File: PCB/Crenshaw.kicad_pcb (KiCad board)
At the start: 2 copper layers, 44.5 x 37 mm, 7 parts, among them J1 In, J2 Out

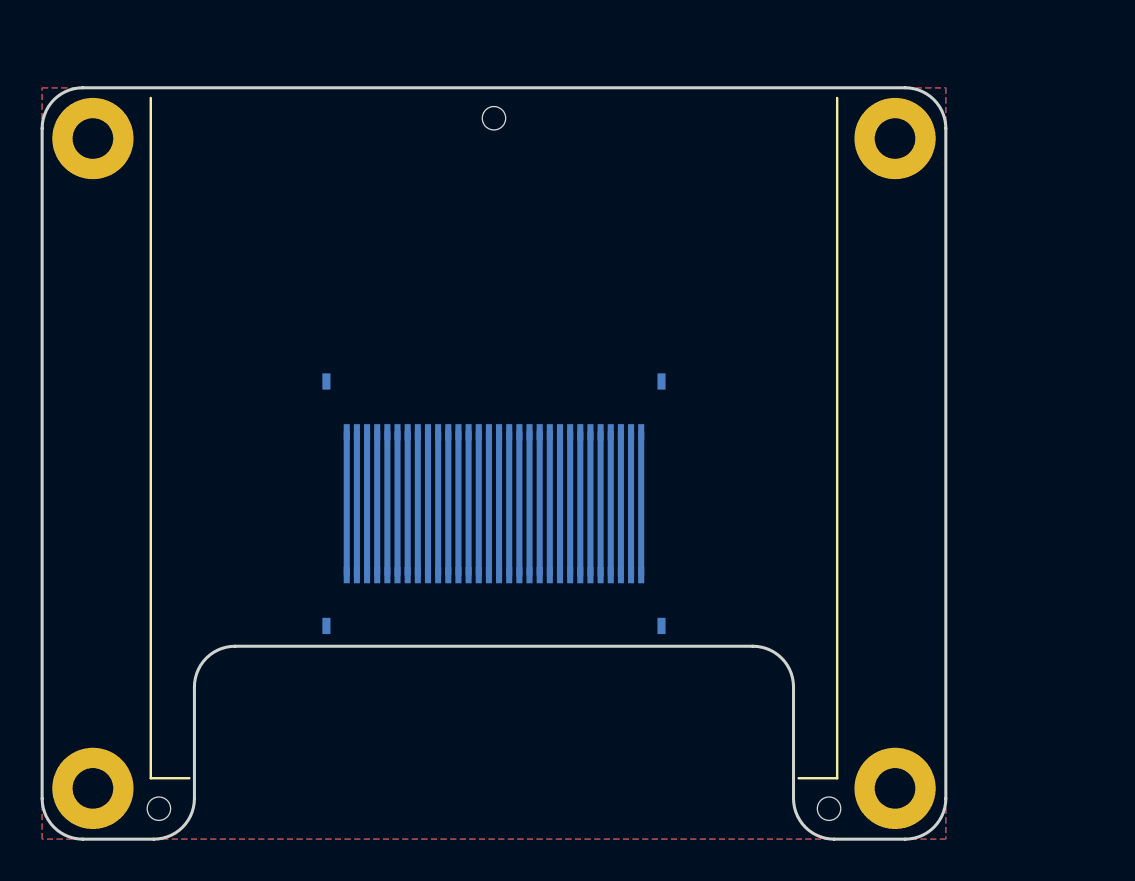
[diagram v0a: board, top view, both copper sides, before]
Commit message: 27/03/2023 update
Added voltage regulator, SSD1351 supporting circuitry and [VIK](https://github.com/sadekbaroudi/vik) connector. Added license. Added metadata to schematic and board files. Added VIK module certification card.
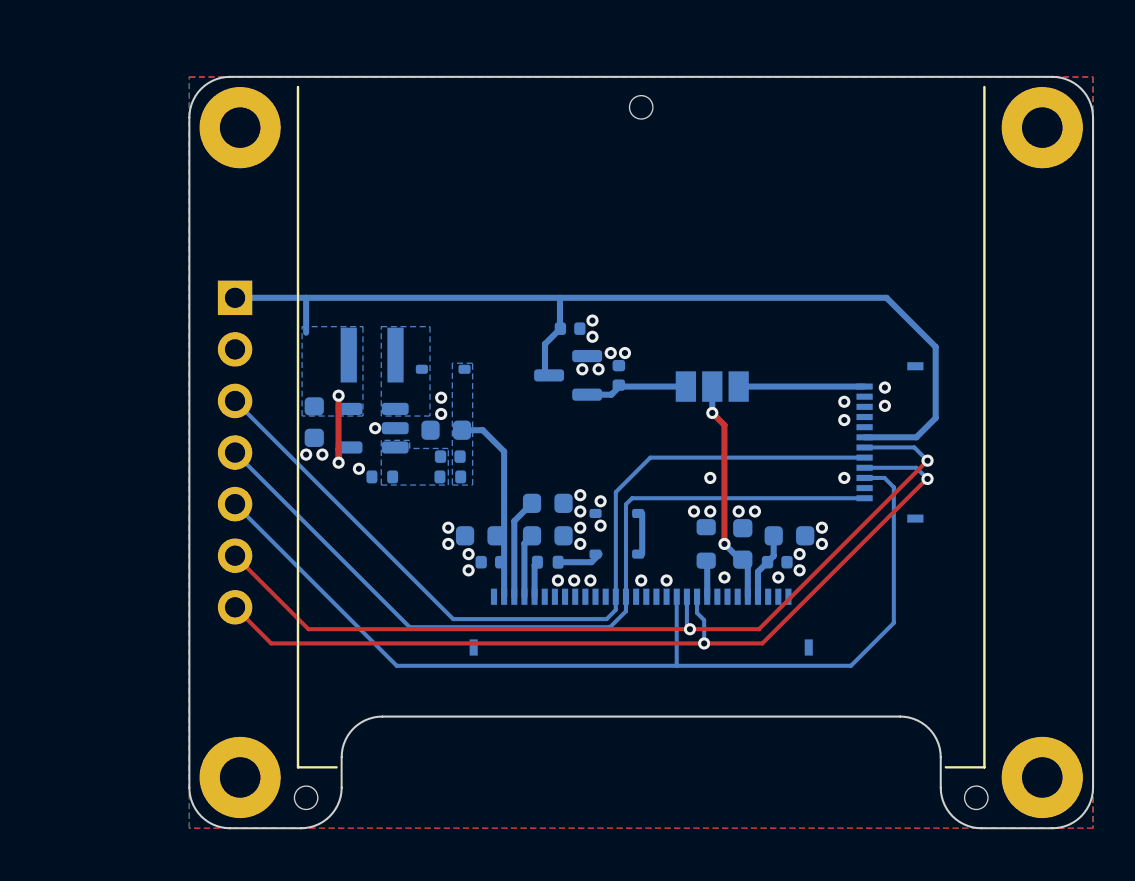
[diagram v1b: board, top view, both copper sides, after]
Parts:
- removed the H1 at (47.8, 40.5)
- added A2: VIK logo, Crenshaw:vik-logo-small, B.Cu at (71.1, 47.3)
- added C1: 100n, Capacitor_SMD:C_0402_1005Metric, B.Cu at (47.6, 45.4)
- added C10: 4u7, Capacitor_SMD:C_0603_1608Metric, B.Cu at (45.4, 38.9)
- added C11: 1u, Capacitor_SMD:C_0402_1005Metric, B.Cu at (51.5, 33.9)
- added C12: 1u, Capacitor_SMD:C_0402_1005Metric, B.Cu at (53.9, 36.2)
- added C2: 10u, Capacitor_SMD:C_0603_1608Metric, B.Cu at (47.1, 44.1)
- added C3: 1u, Capacitor_SMD:C_0603_1608Metric, B.Cu at (50.4, 42.5)
- added C4: 1u, Capacitor_SMD:C_0603_1608Metric, B.Cu at (50.4, 44.1)
- added C5: 1u, Capacitor_SMD:C_0603_1608Metric, B.Cu at (60.0, 44.5)
- added C6: 100n, Capacitor_SMD:C_0402_1005Metric, B.Cu at (61.7, 45.4)
- added C7: 1u, Capacitor_SMD:C_0603_1608Metric, B.Cu at (62.3, 44.1)
- added C8: 4u7, Capacitor_SMD:C_0603_1608Metric, B.Cu at (38.9, 38.5)
- added C9: 22p, Capacitor_SMD:C_0402_1005Metric, B.Cu at (45.6, 40.2)
- added D1: 1N4148, Diode_SMD:D_SOD-323, B.Cu at (53.8, 45.0)
- added D2: 1N4148, Diode_SMD:D_SOD-323, B.Cu at (53.8, 43.0)
- added D3: 1N5819WS, Diode_SMD:D_SOD-323, B.Cu at (45.2, 35.9)
- added J3: VIK Module, Crenshaw:vik-module-connector-horizontal, B.Cu at (68.5, 39.5)
- added JP1: 3V3 SEL, Jumper:SolderJumper-3_P1.3mm_Open_Pad1.0x1.5mm_NumberLabels, B.Cu at (58.5, 36.8)
- added L1: 10u, Inductor_SMD:L_Sunlord_SWPA3012S, B.Cu at (41.8, 35.2)
- added R1: 51, Resistor_SMD:R_0402_1005Metric, B.Cu at (50.4, 45.4)
- added R2: 560k, Resistor_SMD:R_0603_1608Metric, B.Cu at (58.2, 44.5)
- added R4: 1M, Resistor_SMD:R_0402_1005Metric, B.Cu at (45.6, 41.2)
- added R5: 100k, Resistor_SMD:R_0402_1005Metric, B.Cu at (42.2, 41.2)
- added U1: TPS61040DBV, Package_TO_SOT_SMD:SOT-23-5, B.Cu at (41.8, 38.8)
- added U2: XC6206P332MR, Package_TO_SOT_SMD:SOT-23, B.Cu at (51.4, 36.2)
- J1: value In -> OLED_Breakout; footprint Crenshaw:HRS_FH34SRJ-30S-0.5SH(50) -> Crenshaw:OLED_1.5_SSD1351_128x128; moved to F.Cu
- J2: value Out -> SSD1351
- moved J1 8.05 mm to (55.0, 40.0)
- moved A1 7.41 mm to (55.0, 26.2)
- moved J2 7.33 mm to (55.0, 49.6)
- moved H1 7.27 mm to (55.0, 23.0)
- moved H2 7.27 mm to (71.5, 57.0)
- moved H3 7.27 mm to (38.5, 57.0)
- renumbered H2 to H1, H3 to H2, H4 to H3
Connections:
- J1 pad 1: Net-(J1-Pin_1) -> +5V
- J1 pad 2: Net-(J1-Pin_2) -> GND
- J1 pad 3: Net-(J1-Pin_3) -> MOSI
- J1 pad 4: Net-(J1-Pin_4) -> SCK
- J1 pad 5: Net-(J1-Pin_5) -> CS
- J1 pad 6: Net-(J1-Pin_6) -> DC
- J1 pad 7: Net-(J1-Pin_7) -> ~{RST}
- J1 pad MP: GND -> (no net)
- J2 pad 1: Net-(J1-Pin_30) -> GND
- J2 pad 10: Net-(J1-Pin_21) -> GND
- J2 pad 11: Net-(J1-Pin_20) -> GND
- J2 pad 12: Net-(J1-Pin_19) -> unconnected-(J2-D2-Pad12)
- J2 pad 13: Net-(J1-Pin_18) -> MOSI
- J2 pad 14: Net-(J1-Pin_17) -> SCK
- J2 pad 15: Net-(J1-Pin_16) -> GND
- J2 pad 16: Net-(J1-Pin_15) -> GND
- J2 pad 17: Net-(J1-Pin_14) -> unconnected-(J2-BS0-Pad17)
- J2 pad 18: Net-(J1-Pin_13) -> GND
- J2 pad 19: Net-(J1-Pin_12) -> CS
- J2 pad 2: Net-(J1-Pin_29) -> +13V
- J2 pad 20: Net-(J1-Pin_11) -> DC
- J2 pad 21: Net-(J1-Pin_10) -> ~{RST}
- J2 pad 22: Net-(J1-Pin_9) -> Net-(J2-IREF)
- J2 pad 23: Net-(J1-Pin_8) -> unconnected-(J2-GPIO1-Pad23)
- J2 pad 24: Net-(J1-Pin_7) -> unconnected-(J2-GPIO0-Pad24)
- J2 pad 25: Net-(J1-Pin_6) -> unconnected-(J2-NC-Pad25)
- J2 pad 26: Net-(J1-Pin_5) -> +3V3
- J2 pad 27: Net-(J1-Pin_4) -> Net-(J2-VCI)
- J2 pad 28: Net-(J1-Pin_3) -> GND
- J2 pad 29: Net-(J1-Pin_2) -> unconnected-(J2-NC-Pad29)
- J2 pad 3: Net-(J1-Pin_28) -> Net-(J2-VCOMH)
- J2 pad 30: Net-(J1-Pin_1) -> GND
- J2 pad 4: Net-(J1-Pin_27) -> Net-(J2-VDDIO)
- J2 pad 5: Net-(J1-Pin_26) -> Net-(J2-VSL)
- J2 pad 6: Net-(J1-Pin_25) -> unconnected-(J2-NC-Pad6)
- J2 pad 7: Net-(J1-Pin_24) -> GND
- J2 pad 8: Net-(J1-Pin_23) -> GND
- J2 pad 9: Net-(J1-Pin_22) -> GND
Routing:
- net +5V: track 0.00 -> 52.7 mm, vias 0 -> 2
- net CS: track 0.00 -> 48.3 mm
- net DC: track 0.00 -> 44.1 mm, vias 0 -> 2
- net ~{RST}: track 0.00 -> 44.0 mm, vias 0 -> 2
- net MOSI: track 0.00 -> 42.1 mm
- net SCK: track 0.00 -> 40.3 mm
- net +3V3: track 0.00 -> 11.0 mm, vias 0 -> 2
- net +13V: track 0.00 -> 9.66 mm
- net Net-(J1-Pin_9): track 7.04 -> 0.00 mm
- net Net-(J1-Pin_8): track 7.04 -> 0.00 mm
- net Net-(J1-Pin_7): track 7.04 -> 0.00 mm
- net Net-(J1-Pin_6): track 7.04 -> 0.00 mm
- net Net-(J1-Pin_4): track 7.04 -> 0.00 mm
- net Net-(J1-Pin_30): track 7.04 -> 0.00 mm
- net Net-(J1-Pin_3): track 7.04 -> 0.00 mm
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- added copper zone on B.Cu, net +13V
- added copper zone on B.Cu, net +5V
- added copper zone on B.Cu, net Net-(D3-A)
- added copper zone on B.Cu, net Net-(U1-FB)
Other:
- outline, holes or cut-outs redrawn
- rule pad_to_mask_clearance: 0.102 -> 0
- board text added: "3V3"
- board text added: "LDO"
- board text added: "VIK"

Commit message: 28/07/2023 update
Added pin labels. Added VIK size row to certification card.
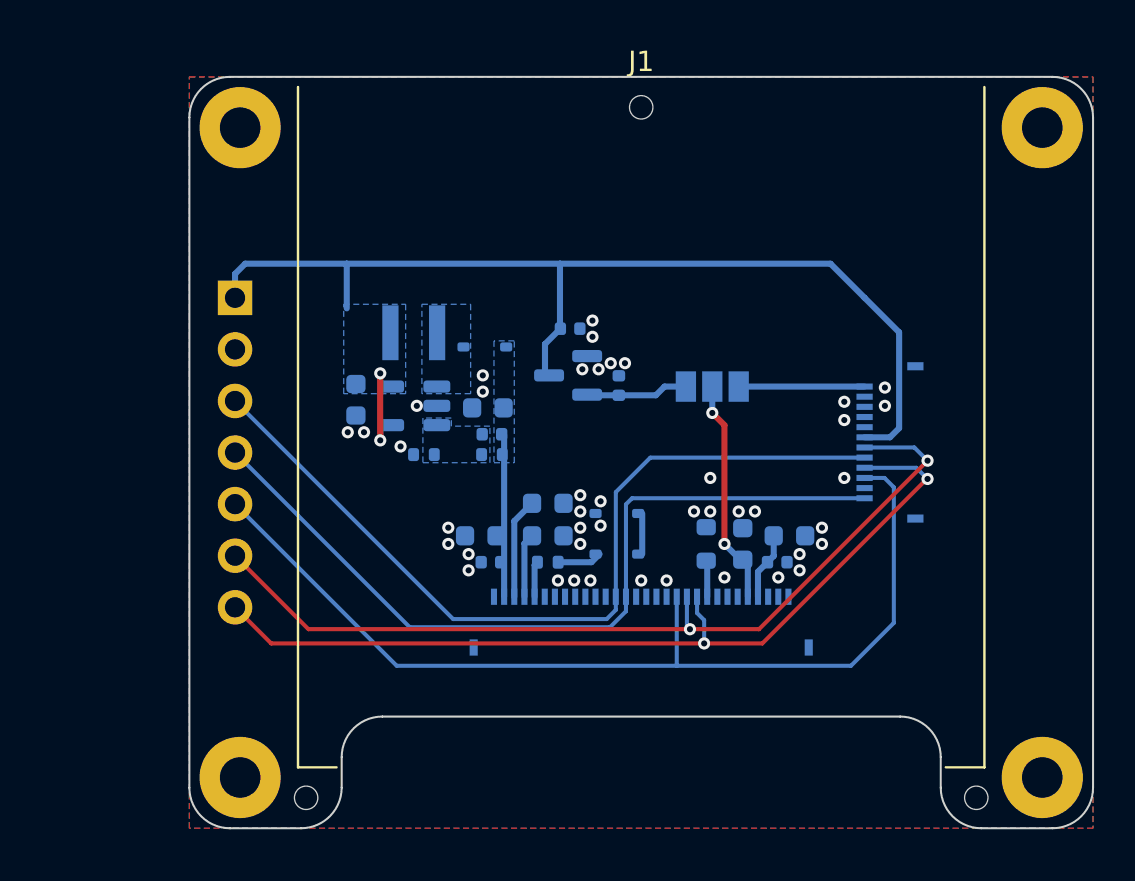
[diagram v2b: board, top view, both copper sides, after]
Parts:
- moved A2 2.80 mm to (68.3, 47.4)
- moved C10 2.33 mm to (47.5, 37.8)
- moved C8 2.33 mm to (41.0, 37.4)
- moved C9 2.33 mm to (47.6, 39.1)
- moved D3 2.33 mm to (47.3, 34.8)
- moved L1 2.33 mm to (43.8, 34.1)
- moved R4 2.33 mm to (47.6, 40.1)
- moved R5 2.33 mm to (44.3, 40.1)
- moved U1 2.33 mm to (43.8, 37.7)
- moved C12 0.50 mm to (53.9, 36.7)
- moved A1 0.40 mm to (55.0, 25.8)
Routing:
- net +13V: track 9.66 -> 7.95 mm
- net +5V: track 52.7 -> 54.1 mm

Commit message: 04/08/2023 update
Changed VIK and OLED FFC to FH12. Stitched ground planes together. Fixed VIK footprint. Moved production files to easier to access location.
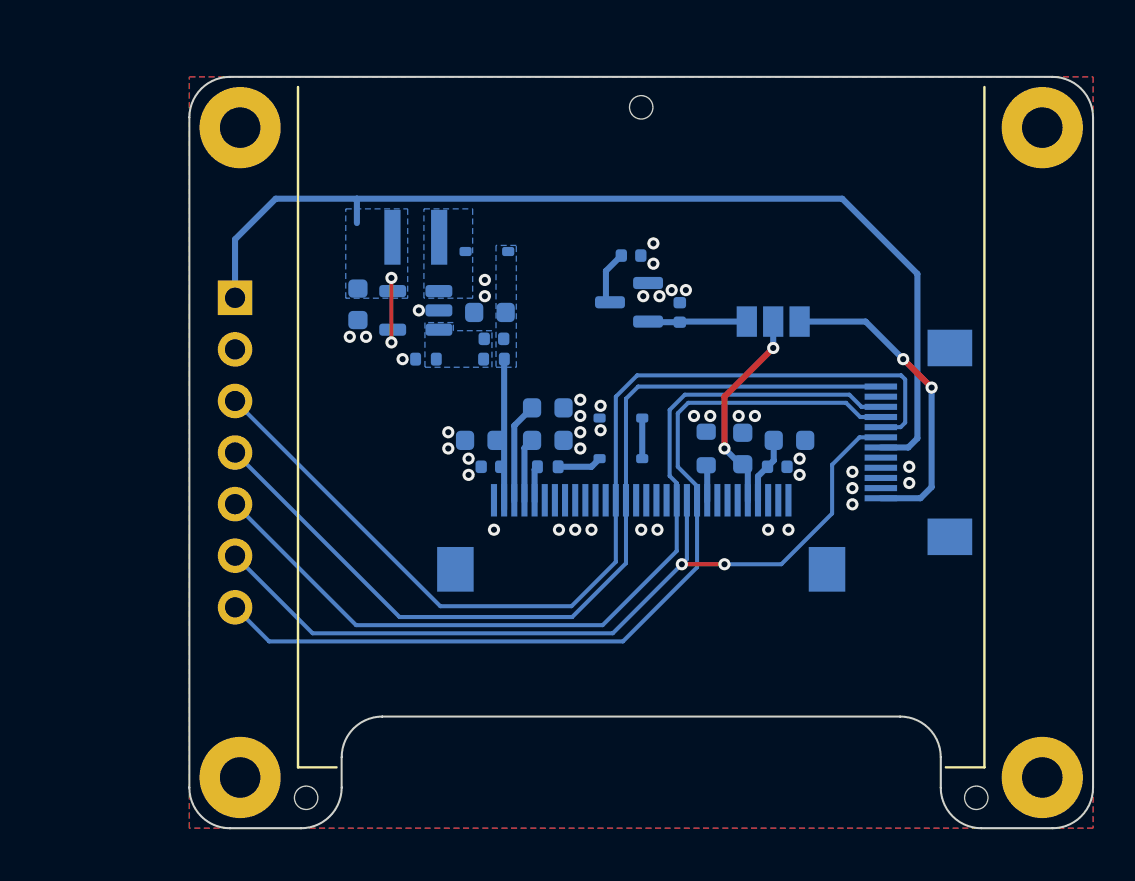
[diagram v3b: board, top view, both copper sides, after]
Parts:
- A1: footprint Crenshaw:Ariamelon_Logo_x3_CU -> Crenshaw:Ariamelon_Logo_x2_Mask
- J2: footprint Crenshaw:HRS_FH34SRJ-30S-0.5SH(50) -> Crenshaw:Hirose_FH12-30S-0.5SH_1x30-1MP_P0.50mm_Horizontal
- moved A1 7.68 mm to (62.6, 24.7)
- moved J2 5.25 mm to (55.0, 44.4)
- moved D1 4.70 mm to (54.0, 40.3)
- moved D2 4.70 mm to (54.0, 38.3)
- moved L1 4.70 mm to (43.9, 29.4)
- moved C9 4.70 mm to (47.8, 34.4)
- moved D3 4.70 mm to (47.4, 30.1)
- moved R4 4.70 mm to (47.8, 35.4)
- moved R5 4.70 mm to (44.4, 35.4)
- moved U1 4.70 mm to (43.9, 33.0)
- moved C10 4.70 mm to (47.5, 33.1)
- moved C8 4.70 mm to (41.0, 32.7)
- moved C2 4.70 mm to (47.1, 39.4)
- moved C3 4.70 mm to (50.4, 37.8)
- moved C4 4.70 mm to (50.4, 39.4)
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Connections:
- J2 pad 10: GND -> ~{RST}
- J2 pad 11: GND -> DC
- J2 pad 12: unconnected-(J2-D2-Pad12) -> CS
- J2 pad 13: MOSI -> GND
- J2 pad 14: SCK -> unconnected-(J2-BS0-Pad14)
- J2 pad 17: unconnected-(J2-BS0-Pad17) -> SCK
- J2 pad 18: GND -> MOSI
- J2 pad 19: CS -> unconnected-(J2-D2-Pad19)
- J2 pad 2: +13V -> unconnected-(J2-NC-Pad2)
- J2 pad 20: DC -> GND
- J2 pad 21: ~{RST} -> GND
- J2 pad 22: Net-(J2-IREF) -> GND
- J2 pad 23: unconnected-(J2-GPIO1-Pad23) -> GND
- J2 pad 24: unconnected-(J2-GPIO0-Pad24) -> GND
- J2 pad 26: +3V3 -> Net-(J2-VSL)
- J2 pad 27: Net-(J2-VCI) -> Net-(J2-VDDIO)
- J2 pad 28: GND -> Net-(J2-VCOMH)
- J2 pad 29: unconnected-(J2-NC-Pad29) -> +13V
- J2 pad 3: Net-(J2-VCOMH) -> GND
- J2 pad 4: Net-(J2-VDDIO) -> Net-(J2-VCI)
- J2 pad 5: Net-(J2-VSL) -> +3V3
- J2 pad 7: GND -> unconnected-(J2-GPIO0-Pad7)
- J2 pad 8: GND -> unconnected-(J2-GPIO1-Pad8)
- J2 pad 9: GND -> Net-(J2-IREF)
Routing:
- net +3V3_VIK: track 6.15 -> 15.5 mm, vias 0 -> 2
- net MOSI: track 42.1 -> 50.2 mm
- net SCK: track 40.3 -> 45.0 mm
- net CS: track 48.3 -> 44.7 mm
- net +5V: track 54.1 -> 56.5 mm
- net DC: track 44.1 -> 41.9 mm
- net +3V3: track 11.0 -> 10.3 mm
- net +13V: track 7.95 -> 7.39 mm
- net ~{RST}: track 44.0 -> 44.5 mm, vias 2 -> 0
- net GND: vias 43 -> 41
